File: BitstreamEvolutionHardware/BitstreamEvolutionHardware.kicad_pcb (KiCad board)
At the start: 2 copper layers, 25 x 25 mm, 1 part

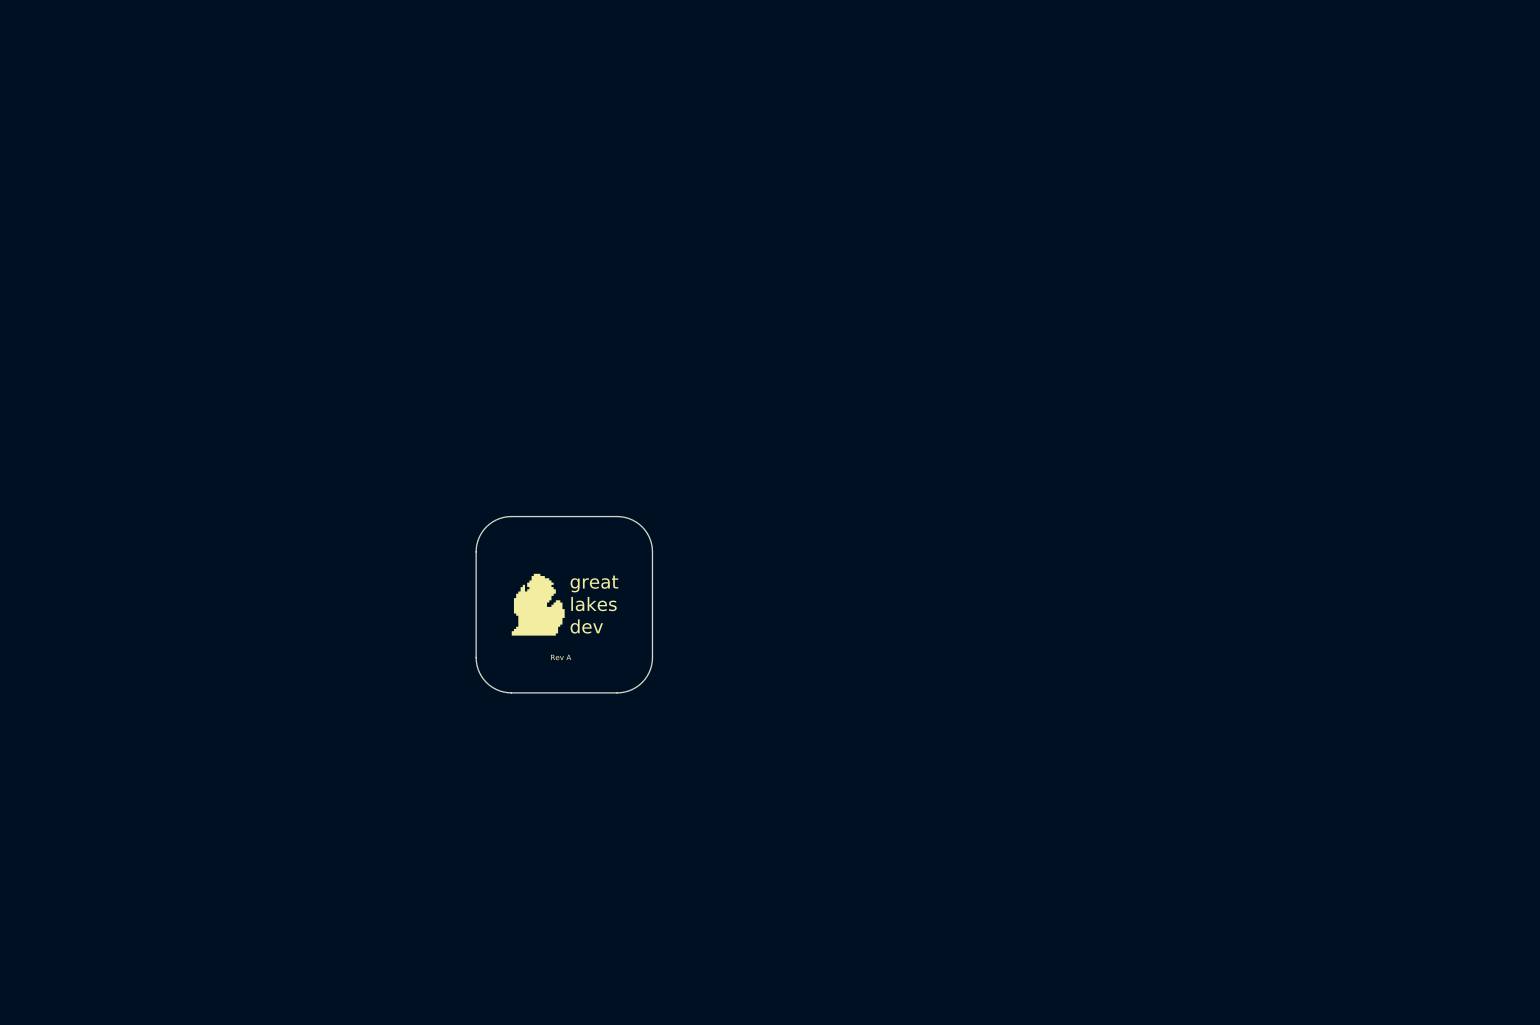
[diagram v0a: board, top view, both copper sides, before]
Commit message: Added Connectors Section to Sch and Linked Footprints
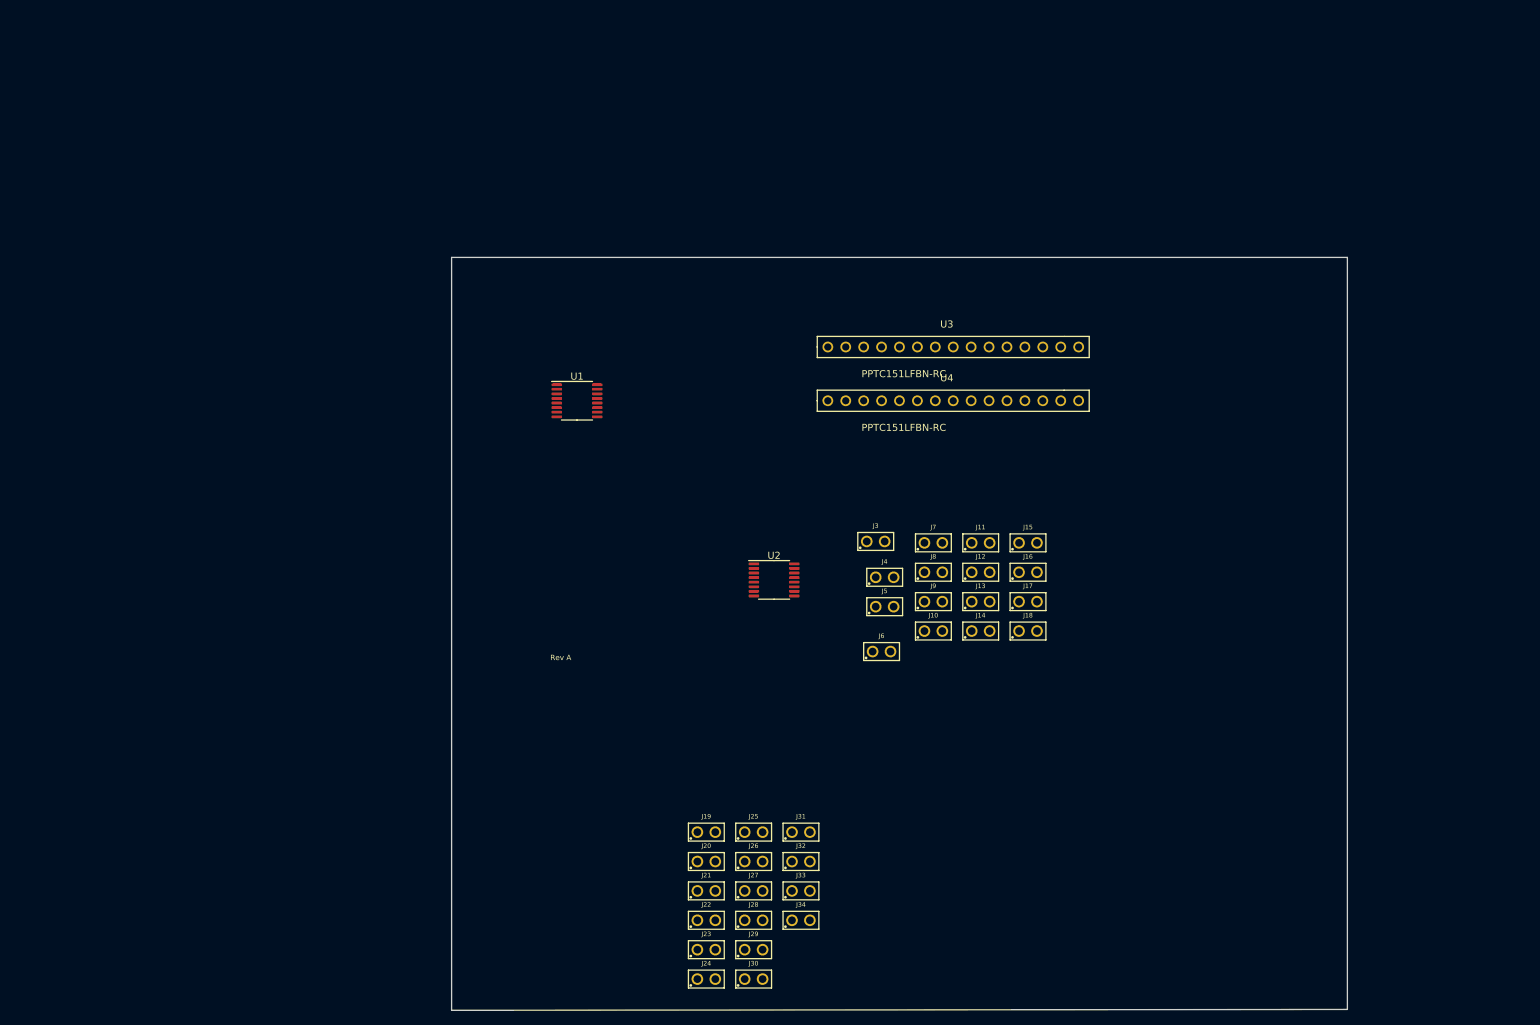
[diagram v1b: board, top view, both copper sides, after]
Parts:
- removed G***: LOGO, gld:gld-logo
- added J10: 61300211121, footprints:61300211121, F.Cu at (164.8, 101.2)
- added J11: 61300211121, footprints:61300211121, F.Cu at (171.5, 88.7)
- added J12: 61300211121, footprints:61300211121, F.Cu at (171.5, 92.9)
- added J13: 61300211121, footprints:61300211121, F.Cu at (171.5, 97.1)
- added J14: 61300211121, footprints:61300211121, F.Cu at (171.5, 101.2)
- added J15: 61300211121, footprints:61300211121, F.Cu at (178.2, 88.7)
- added J16: 61300211121, footprints:61300211121, F.Cu at (178.2, 92.9)
- added J17: 61300211121, footprints:61300211121, F.Cu at (178.2, 97.1)
- added J18: 61300211121, footprints:61300211121, F.Cu at (178.2, 101.2)
- added J19: 61300211121, footprints:61300211121, F.Cu at (132.6, 129.7)
- added J20: 61300211121, footprints:61300211121, F.Cu at (132.6, 133.9)
- added J21: 61300211121, footprints:61300211121, F.Cu at (132.6, 138.1)
- added J22: 61300211121, footprints:61300211121, F.Cu at (132.6, 142.2)
- added J23: 61300211121, footprints:61300211121, F.Cu at (132.6, 146.4)
- added J24: 61300211121, footprints:61300211121, F.Cu at (132.6, 150.6)
- added J25: 61300211121, footprints:61300211121, F.Cu at (139.3, 129.7)
- added J26: 61300211121, footprints:61300211121, F.Cu at (139.3, 133.9)
- added J27: 61300211121, footprints:61300211121, F.Cu at (139.3, 138.1)
- added J28: 61300211121, footprints:61300211121, F.Cu at (139.3, 142.2)
- added J29: 61300211121, footprints:61300211121, F.Cu at (139.3, 146.4)
- added J3: 61300211121, footprints:61300211121, F.Cu at (156.7, 88.5)
- added J30: 61300211121, footprints:61300211121, F.Cu at (139.3, 150.6)
- added J31: 61300211121, footprints:61300211121, F.Cu at (146.1, 129.7)
- added J32: 61300211121, footprints:61300211121, F.Cu at (146.1, 133.9)
- added J33: 61300211121, footprints:61300211121, F.Cu at (146.1, 138.1)
- added J34: 61300211121, footprints:61300211121, F.Cu at (146.1, 142.2)
- added J4: 61300211121, footprints:61300211121, F.Cu at (157.9, 93.6)
- added J5: 61300211121, footprints:61300211121, F.Cu at (157.9, 97.8)
- added J6: 61300211121, footprints:61300211121, F.Cu at (157.5, 104.1)
- added J7: 61300211121, footprints:61300211121, F.Cu at (164.8, 88.7)
- added J8: 61300211121, footprints:61300211121, F.Cu at (164.8, 92.9)
- added J9: 61300211121, footprints:61300211121, F.Cu at (164.8, 97.1)
- added U1: ADS7828, Package_SO:TSSOP-16_4.4x5mm_P0.65mm, F.Cu at (114.3, 68.6)
- added U2: ADS7828, Package_SO:TSSOP-16_4.4x5mm_P0.65mm, F.Cu at (142.2, 94.0)
- added U3: PPTC151LFBN-RC, footprints:PPTC151LFBN-RC, F.Cu at (149.9, 61.0)
- added U4: PPTC151LFBN-RC, footprints:PPTC151LFBN-RC, F.Cu at (149.9, 68.6)
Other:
- board size 25 x 25 mm -> 127 x 106.7 mm

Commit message: Rev 0.1 Rough Draft Done
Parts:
- added J1: PPPC101LFBN-RC, footprints:PPPC101LFBN-RC, F.Cu at (96.3, 87.6)
- added J2: PPPC101LFBN-RC, footprints:PPPC101LFBN-RC, F.Cu at (111.8, 87.6)
- added J35: 61300211121, footprints:61300211121, F.Cu at (61.8, 73.4)
- added J36: 61300211121, footprints:61300211121, F.Cu at (110.2, 33.5)
- added J37: 61300211121, footprints:61300211121, F.Cu at (91.8, 33.5)
- added J38: 61300211121, footprints:61300211121, F.Cu at (141.7, 35.1)
- added J39: 61300211121, footprints:61300211121, F.Cu at (144.6, 80.2)
- added R1: 2K, Resistor_SMD:R_0201_0603Metric, F.Cu at (62.4, 65.8)
- added R10: 2K, Resistor_SMD:R_0201_0603Metric, F.Cu at (84.3, 27.7)
- added R11: 2K, Resistor_SMD:R_0201_0603Metric, F.Cu at (134.1, 29.0)
- added R12: 2K, Resistor_SMD:R_0201_0603Metric, F.Cu at (136.7, 29.0)
- added R2: 2K, Resistor_SMD:R_0201_0603Metric, F.Cu at (65.9, 65.8)
- added R3: 5K, Resistor_SMD:R_0201_0603Metric, F.Cu at (65.4, 79.5)
- added R4: 5K, Resistor_SMD:R_0201_0603Metric, F.Cu at (145.3, 73.4)
- added R5: 2K, Resistor_SMD:R_0201_0603Metric, F.Cu at (142.8, 73.7)
- added R6: 2K, Resistor_SMD:R_0201_0603Metric, F.Cu at (142.8, 75.5)
- added R7: 2K, Resistor_SMD:R_0201_0603Metric, F.Cu at (104.1, 28.2)
- added R8: 2K, Resistor_SMD:R_0201_0603Metric, F.Cu at (106.7, 28.2)
- added R9: 2K, Resistor_SMD:R_0201_0603Metric, F.Cu at (82.6, 27.7)
- added U5: MAX5820MEUA+, footprints:MAX5820MEUA&plus_, F.Cu at (101.6, 33.5)
- added U6: MAX5820MEUA+, footprints:MAX5820MEUA&plus_, F.Cu at (81.6, 33.5)
- added U7: AD9833BRMZ, footprints:SOP50P490X110-10N, F.Cu at (129.0, 36.3)
- added Y1: XRCGB25M000F3M04R0, footprints:OSC_XRCGB25M000F3M04R0, F.Cu at (120.9, 35.6)
- moved U3 114.4 mm to (40.8, 26.4), turned to -90 degrees
- moved U4 105.2 mm to (53.5, 26.4), turned to -90 degrees
- moved J29 96.5 mm to (125.0, 51.0), turned to 180 degrees
- moved J15 95.6 mm to (82.8, 93.9)
- moved J18 95.5 mm to (82.8, 97.3)
- moved J17 95.5 mm to (82.8, 100.7)
- moved J16 95.5 mm to (82.8, 90.5)
- moved J6 92.5 mm to (82.8, 49.5)
- moved J14 90.4 mm to (82.8, 83.7)
- moved J34 90.3 mm to (125.0, 54.5), turned to 180 degrees
- moved J12 90.2 mm to (82.8, 76.8)
- moved J13 89.3 mm to (82.8, 87.1)
- moved J11 89.1 mm to (82.8, 80.3)
- moved J10 87.8 mm to (82.8, 70.0)
- moved J8 87.2 mm to (82.8, 63.2)
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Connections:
- U1 pad 10: unconnected-(U1-REF-Pad10) -> /ADC_REF_B
- U1 pad 12: unconnected-(U1-A0-Pad12) -> /Arduino_+3.3V
- U1 pad 13: unconnected-(U1-A1-Pad13) -> /Arduino_+3.3V
- U1 pad 14: unconnected-(U1-SCL-Pad14) -> /Arduino_SCL
- U1 pad 15: unconnected-(U1-SDA-Pad15) -> /Arduino_SDA
- U1 pad 16: unconnected-(U1-VDD-Pad16) -> /Arduino_+3.3V
- U1 pad 9: unconnected-(U1-GND-Pad9) -> GND
- U2 pad 10: unconnected-(U2-REF-Pad10) -> /ADC_REF_A
- U2 pad 12: unconnected-(U2-A0-Pad12) -> GND
- U2 pad 13: unconnected-(U2-A1-Pad13) -> GND
- U2 pad 14: unconnected-(U2-SCL-Pad14) -> /Arduino_SCL
- U2 pad 15: unconnected-(U2-SDA-Pad15) -> /Arduino_SDA
- U2 pad 16: unconnected-(U2-VDD-Pad16) -> /Arduino_+3.3V
- U2 pad 9: unconnected-(U2-GND-Pad9) -> GND
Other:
- board size 127 x 106.7 mm -> 115.1 x 88.1 mm
- board text added: "A Side"
- board text added: "B Side"
- board text added: "Bitstream Evolution Hardware Rev 0.1"
- board text added: "CH0"
- board text added: "CH1"
- board text added: "CH2"
- board text added: "CH3"
- board text added: "CH4"
- board text added: "CH5"
- board text added: "CH6"
- board text added: "CH7"
- board text added: "DAC A OUTPUT"
- board text added: "DAC B OUTPUT"
- board text added: "DACs"
- board text added: "FPGA"
- board text added: "FPGA 0"
- board text added: "FPGA 1"
- board text added: "FPGA 2"
- board text added: "FPGA 3"
- board text added: "FPGA 4"
- board text added: "FPGA 5"
- board text added: "FPGA 6"
- board text added: "FPGA 7"
- board text added: "NANO"
- board text added: "Waveform Generator"
- board text added: "Waveform Output"

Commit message: Backup
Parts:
- removed R10: 2K, Resistor_SMD:R_0201_0603Metric
- removed U6: MAX5820MEUA+, footprints:MAX5820MEUA&plus_
- added C1: 10uF, Capacitor_SMD:C_0805_2012Metric, F.Cu at (51.8, 91.5)
- added C3: 10uF, Capacitor_SMD:C_0805_2012Metric, F.Cu at (115.8, 30.2)
- added C4: 10uF, Capacitor_SMD:C_0805_2012Metric, F.Cu at (112.3, 34.3)
- added C5: 0.47uF, Resistor_SMD:R_0805_2012Metric, F.Cu at (132.6, 36.1)
- added C6: 0.47uF, Resistor_SMD:R_0805_2012Metric, F.Cu at (126.5, 36.1)
- added C7: 10uF, Capacitor_SMD:C_0805_2012Metric, F.Cu at (83.7, 21.6)
- added C8: 0.1uF, Capacitor_SMD:C_0805_2012Metric, F.Cu at (83.7, 24.1)
- added G***: LOGO, gld:usbIcon, F.Cu at (92.0, 104.9)
- added G***: LOGO, gld:usbIcon, F.Cu at (48.3, 27.8)
- added H1: MountingHole, gld:MountingHole_3.2mm_M3, F.Cu at (41.0, 19.0)
- added H2: MountingHole, gld:MountingHole_3.2mm_M3, F.Cu at (40.6, 109.2)
- added H3: MountingHole, gld:MountingHole_3.2mm_M3, F.Cu at (132.1, 19.1)
- added H4: MountingHole, gld:MountingHole_3.2mm_M3, F.Cu at (129.0, 109.6)
- added J40: 61300211121, footprints:61300211121, F.Cu at (117.3, 23.6)
- added J41: 61300211121, footprints:61300211121, F.Cu at (114.3, 23.6)
- added J42: 61300211121, footprints:61300211121, F.Cu at (94.0, 27.2)
- added J43: 61300211121, footprints:61300211121, F.Cu at (94.0, 23.4)
- added J44: 61300211121, footprints:61300211121, F.Cu at (69.6, 34.5)
- added J45: 61300211121, footprints:61300211121, F.Cu at (69.6, 21.8)
- added Q1: BSS138, Package_TO_SOT_SMD:SOT-23, F.Cu at (122.0, 33.8)
- added Q2: BSS138, Package_TO_SOT_SMD:SOT-23, F.Cu at (117.3, 37.8)
- added R13: 10K, Resistor_SMD:R_0805_2012Metric, F.Cu at (117.3, 33.8)
- added R14: 10K, Resistor_SMD:R_0805_2012Metric, F.Cu at (120.4, 30.2)
- added R15: 0, Resistor_SMD:R_0805_2012Metric, F.Cu at (46.2, 85.2)
- added R16: 0, Resistor_SMD:R_0805_2012Metric, F.Cu at (42.2, 85.1)
- added R17: 0, Resistor_SMD:R_0805_2012Metric, F.Cu at (42.2, 81.6)
- added R18: 0, Resistor_SMD:R_0805_2012Metric, F.Cu at (46.2, 81.7)
- added R19: 0, Resistor_SMD:R_0201_0603Metric, F.Cu at (122.0, 100.9)
- added R20: 0, Resistor_SMD:R_0201_0603Metric, F.Cu at (124.5, 95.6)
- added R21: 0, Resistor_SMD:R_0201_0603Metric, F.Cu at (124.5, 97.4)
- added R22: 0, Resistor_SMD:R_0201_0603Metric, F.Cu at (124.5, 99.1)
- added U8: Si5351A-B-GT, Package_SO:MSOP-10_3x3mm_P0.5mm, F.Cu at (129.5, 36.1)
- J1, J2: value PPPC101LFBN-RC -> CONN10_N-RC_SUL
- R1, R2, R3: footprint Resistor_SMD:R_0201_0603Metric -> Resistor_SMD:R_0805_2012Metric
- R11, R12: value 2K -> 10K; footprint Resistor_SMD:R_0201_0603Metric -> Resistor_SMD:R_0805_2012Metric
- R7, R8, R9: value 2K -> 4.7K; footprint Resistor_SMD:R_0201_0603Metric -> Resistor_SMD:R_0805_2012Metric
- U5: value MAX5820MEUA+ -> MCP4728; footprint footprints:MAX5820MEUA&plus_ -> Package_SO:MSOP-10_3x3mm_P0.5mm
- U7: value AD9833BRMZ -> RT9193-33GB; footprint footprints:SOP50P490X110-10N -> footprints:SOT94P279X129-5N
- Y1: value XRCGB25M000F3M04R0 -> ABM8G-25.000MHZ-4Y-T3; footprint footprints:OSC_XRCGB25M000F3M04R0 -> footprints:XTAL_ABM8G-25.000MHZ-4Y-T3
- moved J29 60.6 mm to (110.5, 109.9)
- moved J30 53.4 mm to (110.8, 51.9)
- moved J34 48.8 mm to (110.8, 101.2)
- moved J23 46.7 mm to (110.8, 55.4)
- moved J19 41.8 mm to (110.8, 97.2)
- moved J31 40.1 mm to (110.8, 58.8)
- moved J22 35.3 mm to (110.8, 93.7)
- moved J24 33.6 mm to (110.8, 62.3)
- moved J38 32.6 mm to (111.3, 23.6), turned to 90 degrees
- moved R2 32.5 mm to (44.2, 90.0)
- moved R1 29.1 mm to (46.2, 90.0)
- moved J21 29.0 mm to (110.8, 90.2)
- moved R8 27.6 mm to (79.8, 21.6), turned to 180 degrees
- moved J32 27.5 mm to (110.8, 65.8)
- moved R7 26.9 mm to (77.3, 29.2), turned to 0 degrees
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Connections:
- J36 pad 1: Net-(U5-OUTB) -> Net-(U5-VOUTA)
- J36 pad 2: Net-(U5-OUTA) -> Net-(J36-Pad2)
- J37 pad 1: Net-(U6-OUTB) -> Net-(U5-VOUTB)
- J37 pad 2: Net-(U6-OUTA) -> Net-(J36-Pad2)
- J38 pad 1: Net-(U7-VOUT) -> Net-(U8-CLK0)
- R11 pad 1: /Arduino_SDA -> /Generator_3V_SCL
- R11 pad 2: Net-(U7-SDATA) -> /Generator_VDD
- R12 pad 1: Net-(U7-SCLK) -> /Generator_3V_SDA
- R12 pad 2: /Arduino_SCL -> /Generator_VDD
- R7 pad 1: /Arduino_SCL -> Net-(J44-Pad2)
- R8 pad 1: /Arduino_SDA -> /Arduino_+5V
- R8 pad 2: Net-(U5-SDA) -> /Arduino_SCL
- R9 pad 1: /Arduino_SCL -> /Arduino_+5V
- R9 pad 2: Net-(U6-SCL) -> /Arduino_SDA
- U1 pad 1: /ADC_B_Channel_0 -> /ADC_B_Channel_7
- U1 pad 12: /Arduino_+3.3V -> Net-(U1-A0)
- U1 pad 13: /Arduino_+3.3V -> Net-(U1-A1)
- U1 pad 2: /ADC_B_Channel_1 -> /ADC_B_Channel_6
- U1 pad 3: /ADC_B_Channel_2 -> /ADC_B_Channel_5
- U1 pad 4: /ADC_B_Channel_3 -> /ADC_B_Channel_4
- U1 pad 5: /ADC_B_Channel_4 -> /ADC_B_Channel_3
- U1 pad 6: /ADC_B_Channel_5 -> /ADC_B_Channel_2
- U1 pad 7: /ADC_B_Channel_6 -> /ADC_B_Channel_1
- U1 pad 8: /ADC_B_Channel_7 -> /ADC_B_Channel_0
- U2 pad 12: GND -> Net-(U2-A0)
- U2 pad 13: GND -> Net-(U2-A1)
- U5 pad 1: /Arduino_+3.3V -> /Arduino_+5V
- U5 pad 2: GND -> /Arduino_SDA
- U5 pad 3: GND -> /Arduino_SCL
- U5 pad 5: Net-(U5-SDA) -> Net-(U5-RDY/~{BSY})
- U5 pad 6: unconnected-(U5-REF-Pad6) -> Net-(U5-VOUTA)
- U5 pad 7: Net-(U5-OUTA) -> Net-(U5-VOUTB)
- U5 pad 8: Net-(U5-OUTB) -> Net-(U5-VOUTC)
- U7 pad 1: unconnected-(U7-COMP-Pad1) -> /Arduino_+5V
- U7 pad 2: /Arduino_+3.3V -> GND
- U7 pad 3: unconnected-(U7-CAP/2.5V-Pad3) -> /Arduino_+5V
- U7 pad 4: GND -> unconnected-(U7-BP-Pad4)
- U7 pad 5: Net-(U7-MCLK) -> /Generator_VDD
- Y1 pad 1: /Arduino_+3.3V -> Net-(U8-XA)
- Y1 pad 2: (no net) -> GND
- Y1 pad 3: Net-(U7-MCLK) -> Net-(U8-XB)
- Y1 pad 4: (no net) -> GND
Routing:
- net /FPGA_A_5: track 0.00 -> 5.00 mm
- net /FPGA_A_3: track 0.00 -> 4.00 mm
- net /FPGA_A_2: track 0.00 -> 4.00 mm
- net /FPGA_A_1: track 0.00 -> 4.00 mm
- net /FPGA_A_0: track 0.00 -> 4.00 mm
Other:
- board size 115.1 x 88.1 mm -> 98.9 x 97 mm
- board text added: "+"
- board text added: "-"
- board text added: "ADC A Ref Voltage"
- board text added: "ADC CH0"
- board text added: "ADC CH1"
- board text added: "ADC CH2"
- board text added: "ADC CH3"
- board text added: "ADC CH4"
- board text added: "ADC CH5"
- board text added: "ADC CH6"
- board text added: "ADC CH7"
- board text added: "Arduino AREF"
- board text added: "Arduino D0"
- board text added: "Arduino D1"
- board text added: "Arduino D2"
- board text added: "Arduino D3"
- board text added: "Arduino D4"
- board text added: "Arduino D5"
- board text added: "Arduino D7"
- board text added: "DAC Outputs"
- board text added: "Generator Output"
- board text added: "LDAC"
- board text added: "Out 1"
- board text added: "Out 2"
- board text added: "Out 3"
- board text added: "Out 4"
- board text added: "RDY"
- board text removed: "${REVISION}"
- board text removed: "DAC A OUTPUT"
- board text removed: "DAC B OUTPUT"
- board text removed: "DACs"
